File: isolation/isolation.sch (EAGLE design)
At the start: 85 parts, among them IC1 XTLV61048DBVR, IC2 SN74HC14PWR, IC3 SN74HCS32BQAR, IC4 SN74HCS08DYYR, IC5 FDN359BN, IC6 FDN359BN, IC7 FDN359BN, IC8 FDN359BN, J1 S4B-PH-K-S(LF)(SN), J2 S4B-PH-K-S(LF)(SN), J3 S2B-PH-K-S(LF)(SN), J4 S2B-PH-K-S(LF)(SN), J5 S2B-PH-K-S(LF)(SN)

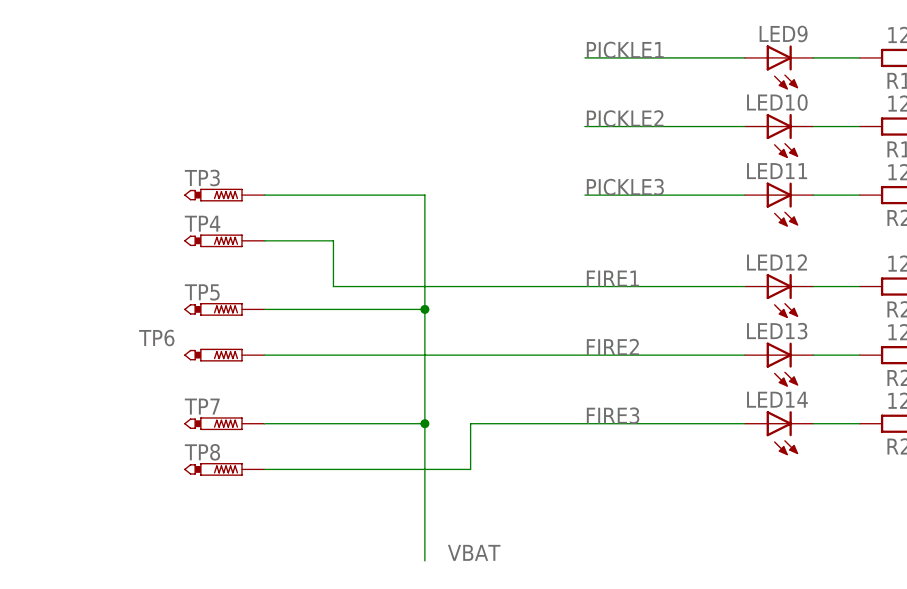
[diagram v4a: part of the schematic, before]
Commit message: placed shrunken components
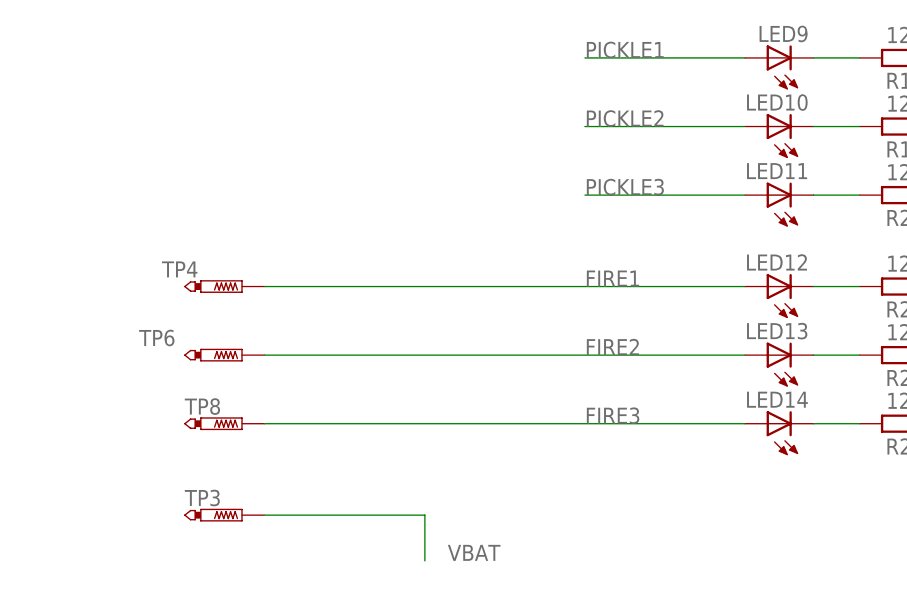
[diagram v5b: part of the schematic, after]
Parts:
- removed TP5, TP7: PTR1PAD1-13, testpad:PTR1PAD1-13
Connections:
- net VBAT: no longer TP5.TP, TP7.TP
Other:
- moved on the sheet: TP3, TP4, TP8
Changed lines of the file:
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@@
 <part name="TP3" library="testpad" library_urn="urn:adsk.eagle:library:385" deviceset="PTR1" device="PAD1-13" package3d_urn="urn:adsk.eagle:package:27946/1"/>
 <part name="TP4" library="testpad" library_urn="urn:adsk.eagle:library:385" deviceset="PTR1" device="PAD1-13" package3d_urn="urn:adsk.eagle:package:27946/1"/>
-<part name="TP5" library="testpad" library_urn="urn:adsk.eagle:library:385" deviceset="PTR1" device="PAD1-13" package3d_urn="urn:adsk.eagle:package:27946/1"/>
 <part name="TP6" library="testpad" library_urn="urn:adsk.eagle:library:385" deviceset="PTR1" device="PAD1-13" package3d_urn="urn:adsk.eagle:package:27946/1"/>
-<part name="TP7" library="testpad" library_urn="urn:adsk.eagle:library:385" deviceset="PTR1" device="PAD1-13" package3d_urn="urn:adsk.eagle:package:27946/1"/>
 <part name="TP8" library="testpad" library_urn="urn:adsk.eagle:library:385" deviceset="PTR1" device="PAD1-13" package3d_urn="urn:adsk.eagle:package:27946/1"/>
 <part name="TP9" library="testpad" library_urn="urn:adsk.eagle:library:385" deviceset="PTR1" device="PAD1-13" package3d_urn="urn:adsk.eagle:package:27946/1"/>
@@
 <attribute name="VALUE" x="96.52" y="-327.66" size="1.778" layer="96"/>
 </instance>
-<instance part="TP3" gate="G$1" x="40.64" y="-401.32" smashed="yes" rot="R270">
-<attribute name="NAME" x="34.29" y="-400.304" size="1.778" layer="95"/>
-<attribute name="TP_SIGNAL_NAME" x="38.1" y="-402.59" size="1.778" layer="97" rot="R270"/>
-</instance>
-<instance part="TP4" gate="G$1" x="40.64" y="-406.4" smashed="yes" rot="R270">
-<attribute name="NAME" x="34.29" y="-405.384" size="1.778" layer="95"/>
-<attribute name="TP_SIGNAL_NAME" x="38.1" y="-407.67" size="1.778" layer="97" rot="R270"/>
-</instance>
-<instance part="TP5" gate="G$1" x="40.64" y="-414.02" smashed="yes" rot="R270">
-<attribute name="NAME" x="34.29" y="-413.004" size="1.778" layer="95"/>
-<attribute name="TP_SIGNAL_NAME" x="38.1" y="-415.29" size="1.778" layer="97" rot="R270"/>
+<instance part="TP3" gate="G$1" x="40.64" y="-436.88" smashed="yes" rot="R270">
+<attribute name="NAME" x="34.29" y="-435.864" size="1.778" layer="95"/>
+<attribute name="TP_SIGNAL_NAME" x="38.1" y="-438.15" size="1.778" layer="97" rot="R270"/>
+</instance>
+<instance part="TP4" gate="G$1" x="40.64" y="-411.48" smashed="yes" rot="R270">
+<attribute name="NAME" x="31.75" y="-410.464" size="1.778" layer="95"/>
+<attribute name="TP_SIGNAL_NAME" x="38.1" y="-412.75" size="1.778" layer="97" rot="R270"/>
 </instance>
 <instance part="TP6" gate="G$1" x="40.64" y="-419.1" smashed="yes" rot="R270">
@@
 <attribute name="TP_SIGNAL_NAME" x="38.1" y="-420.37" size="1.778" layer="97" rot="R270"/>
 </instance>
-<instance part="TP7" gate="G$1" x="40.64" y="-426.72" smashed="yes" rot="R270">
+<instance part="TP8" gate="G$1" x="40.64" y="-426.72" smashed="yes" rot="R270">
 <attribute name="NAME" x="34.29" y="-425.704" size="1.778" layer="95"/>
 <attribute name="TP_SIGNAL_NAME" x="38.1" y="-427.99" size="1.778" layer="97" rot="R270"/>
-</instance>
-<instance part="TP8" gate="G$1" x="40.64" y="-431.8" smashed="yes" rot="R270">
-<attribute name="NAME" x="34.29" y="-430.784" size="1.778" layer="95"/>
-<attribute name="TP_SIGNAL_NAME" x="38.1" y="-433.07" size="1.778" layer="97" rot="R270"/>
 </instance>
 <instance part="TP9" gate="G$1" x="53.34" y="33.02" smashed="yes" rot="R270">
@@
 </segment>
 <segment>
-<wire x1="60.96" y1="-401.32" x2="60.96" y2="-414.02" width="0.1524" layer="91"/>
 <label x="63.5" y="-441.96" size="1.778" layer="95"/>
 <pinref part="TP3" gate="G$1" pin="TP"/>
-<wire x1="60.96" y1="-414.02" x2="60.96" y2="-426.72" width="0.1524" layer="91"/>
-<wire x1="60.96" y1="-426.72" x2="60.96" y2="-441.96" width="0.1524" layer="91"/>
-<wire x1="60.96" y1="-401.32" x2="43.18" y2="-401.32" width="0.1524" layer="91"/>
-<pinref part="TP5" gate="G$1" pin="TP"/>
-<wire x1="43.18" y1="-414.02" x2="60.96" y2="-414.02" width="0.1524" layer="91"/>
-<junction x="60.96" y="-414.02"/>
-<pinref part="TP7" gate="G$1" pin="TP"/>
-<wire x1="43.18" y1="-426.72" x2="60.96" y2="-426.72" width="0.1524" layer="91"/>
-<junction x="60.96" y="-426.72"/>
+<wire x1="60.96" y1="-436.88" x2="60.96" y2="-441.96" width="0.1524" layer="91"/>
+<wire x1="43.18" y1="-436.88" x2="60.96" y2="-436.88" width="0.1524" layer="91"/>
 </segment>
 </net>
@@
 <pinref part="LED12" gate="G$1" pin="A"/>
 <label x="78.74" y="-411.48" size="1.778" layer="95"/>
-<wire x1="96.52" y1="-411.48" x2="50.8" y2="-411.48" width="0.1524" layer="91"/>
-<wire x1="50.8" y1="-411.48" x2="50.8" y2="-406.4" width="0.1524" layer="91"/>
+<wire x1="96.52" y1="-411.48" x2="43.18" y2="-411.48" width="0.1524" layer="91"/>
 <pinref part="TP4" gate="G$1" pin="TP"/>
-<wire x1="50.8" y1="-406.4" x2="43.18" y2="-406.4" width="0.1524" layer="91"/>
 </segment>
 </net>
@@
 <pinref part="LED14" gate="G$1" pin="A"/>
 <label x="78.74" y="-426.72" size="1.778" layer="95"/>
-<wire x1="96.52" y1="-426.72" x2="66.04" y2="-426.72" width="0.1524" layer="91"/>
-<wire x1="66.04" y1="-426.72" x2="66.04" y2="-431.8" width="0.1524" layer="91"/>
+<wire x1="96.52" y1="-426.72" x2="43.18" y2="-426.72" width="0.1524" layer="91"/>
 <pinref part="TP8" gate="G$1" pin="TP"/>
-<wire x1="66.04" y1="-431.8" x2="43.18" y2="-431.8" width="0.1524" layer="91"/>
-</segment>
-</net>
+</segment>
+</net>

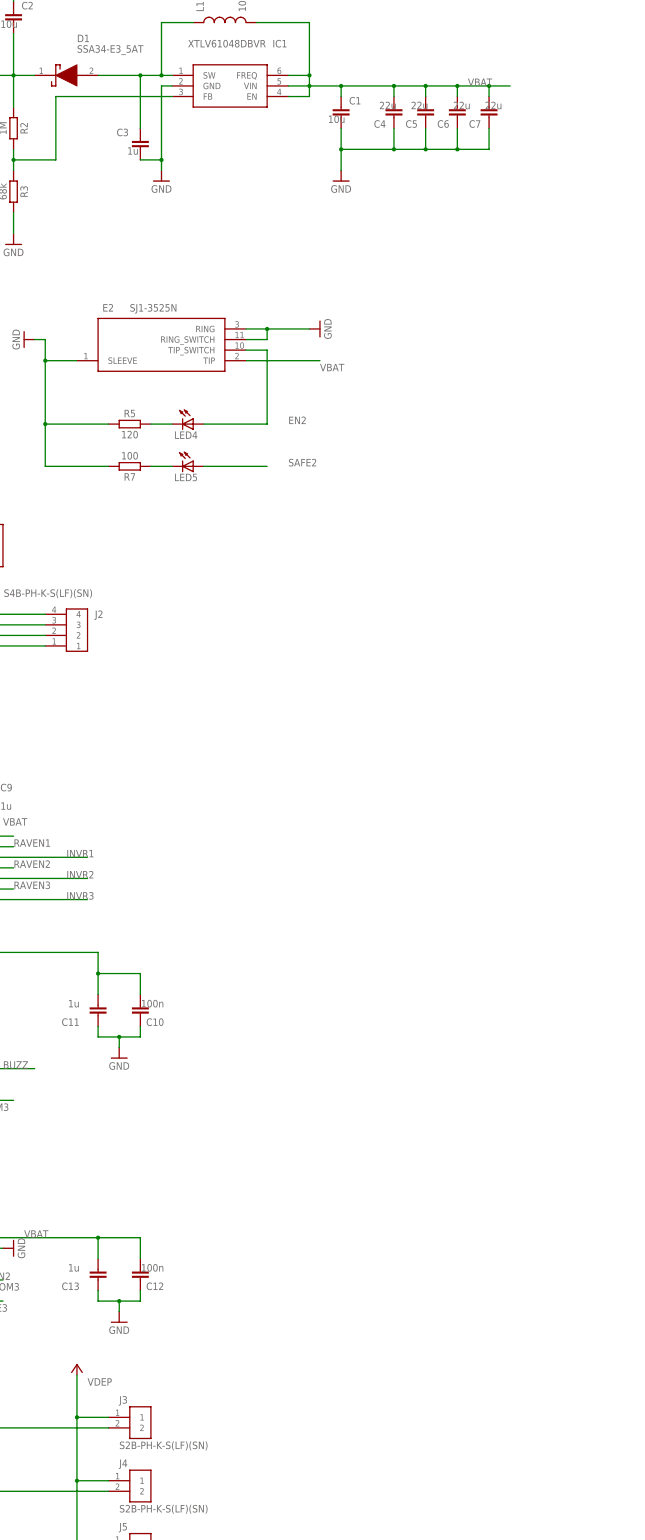
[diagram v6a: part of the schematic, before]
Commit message: add some bulk caps
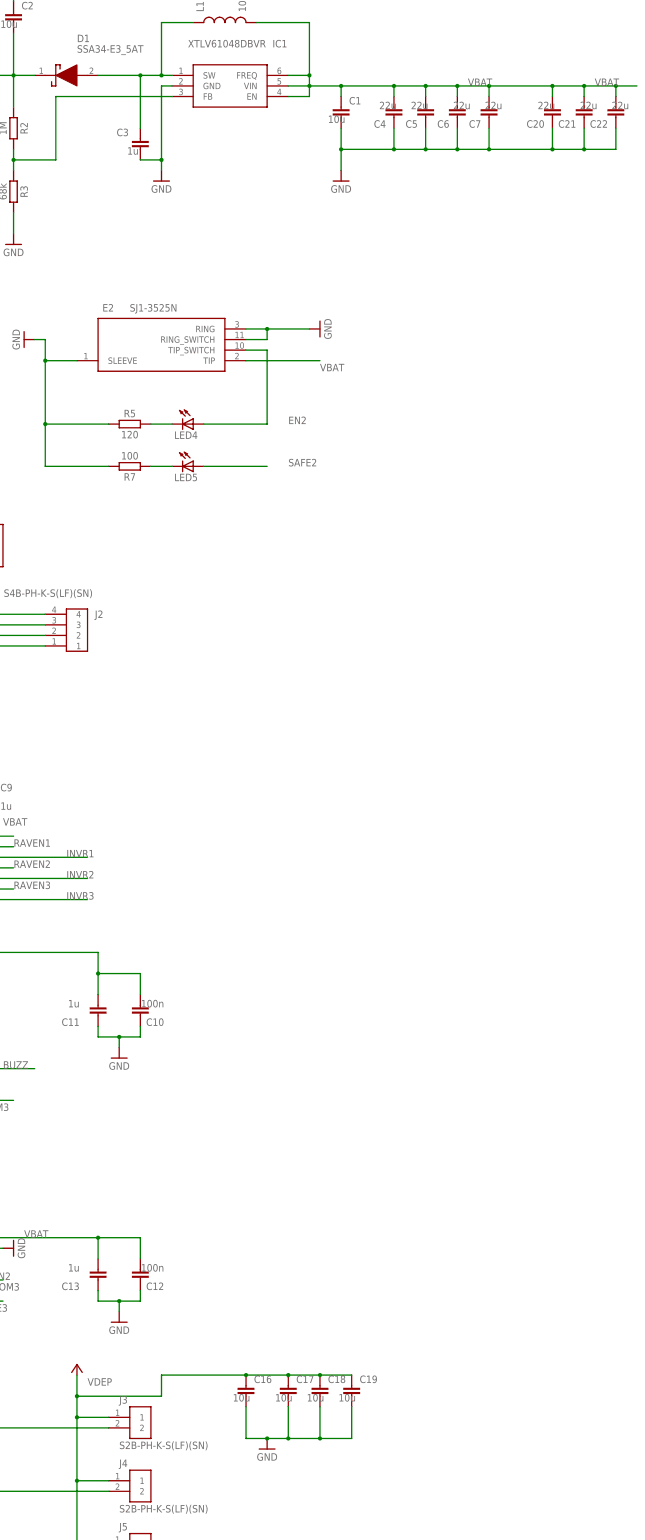
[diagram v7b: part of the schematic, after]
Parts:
- added C16, C17, C18, C19: 10u, Capacitor:C_CHIP-0603(1608-METRIC)
- added C20, C21, C22: 22u, Capacitor:C_CHIP-0603(1608-METRIC)
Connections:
- net GND: now also C16.2, C17.2, C18.2, C19.2, C20.1, C21.1, C22.1
- net VBAT: now also C20.2, C21.2, C22.2
- net VDEP: now also C16.1, C17.1, C18.1, C19.1
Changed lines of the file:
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@@
 <part name="TP8" library="testpad" library_urn="urn:adsk.eagle:library:385" deviceset="PTR1" device="PAD1-13" package3d_urn="urn:adsk.eagle:package:27946/1"/>
 <part name="TP9" library="testpad" library_urn="urn:adsk.eagle:library:385" deviceset="PTR1" device="PAD1-13" package3d_urn="urn:adsk.eagle:package:27946/1"/>
+<part name="C16" library="Capacitor" library_urn="urn:adsk.eagle:library:16290819" deviceset="C" device="CHIP-0603(1608-METRIC)" package3d_urn="urn:adsk.eagle:package:16290898/5" technology="_" value="10u"/>
+<part name="C17" library="Capacitor" library_urn="urn:adsk.eagle:library:16290819" deviceset="C" device="CHIP-0603(1608-METRIC)" package3d_urn="urn:adsk.eagle:package:16290898/5" technology="_" value="10u"/>
+<part name="SUPPLY28" library="Power_Symbols" library_urn="urn:adsk.eagle:library:16502351" deviceset="GND-BAR" device="" value="GND"/>
+<part name="C18" library="Capacitor" library_urn="urn:adsk.eagle:library:16290819" deviceset="C" device="CHIP-0603(1608-METRIC)" package3d_urn="urn:adsk.eagle:package:16290898/5" technology="_" value="10u"/>
+<part name="C19" library="Capacitor" library_urn="urn:adsk.eagle:library:16290819" deviceset="C" device="CHIP-0603(1608-METRIC)" package3d_urn="urn:adsk.eagle:package:16290898/5" technology="_" value="10u"/>
+<part name="C20" library="Capacitor" library_urn="urn:adsk.eagle:library:16290819" deviceset="C" device="CHIP-0603(1608-METRIC)" package3d_urn="urn:adsk.eagle:package:16290898/5" technology="_" value="22u"/>
+<part name="C21" library="Capacitor" library_urn="urn:adsk.eagle:library:16290819" deviceset="C" device="CHIP-0603(1608-METRIC)" package3d_urn="urn:adsk.eagle:package:16290898/5" technology="_" value="22u"/>
+<part name="C22" library="Capacitor" library_urn="urn:adsk.eagle:library:16290819" deviceset="C" device="CHIP-0603(1608-METRIC)" package3d_urn="urn:adsk.eagle:package:16290898/5" technology="_" value="22u"/>
 </parts>
 <sheets>
@@
 <attribute name="NAME" x="46.99" y="34.036" size="1.778" layer="95"/>
 <attribute name="TP_SIGNAL_NAME" x="50.8" y="31.75" size="1.778" layer="97" rot="R270"/>
+</instance>
+<instance part="C16" gate="G$1" x="127" y="-281.94" smashed="yes">
+<attribute name="NAME" x="128.905" y="-281.305" size="1.778" layer="95"/>
+<attribute name="VALUE" x="123.825" y="-285.75" size="1.778" layer="96"/>
+</instance>
+<instance part="C17" gate="G$1" x="137.16" y="-281.94" smashed="yes">
+<attribute name="NAME" x="139.065" y="-281.305" size="1.778" layer="95"/>
+<attribute name="VALUE" x="133.985" y="-285.75" size="1.778" layer="96"/>
+</instance>
+<instance part="SUPPLY28" gate="G$1" x="132.08" y="-297.18" smashed="yes">
+<attribute name="VALUE" x="132.08" y="-299.085" size="1.778" layer="96" align="center"/>
+</instance>
+<instance part="C18" gate="G$1" x="144.78" y="-281.94" smashed="yes">
+<attribute name="NAME" x="146.685" y="-281.305" size="1.778" layer="95"/>
+<attribute name="VALUE" x="141.605" y="-285.75" size="1.778" layer="96"/>
+</instance>
+<instance part="C19" gate="G$1" x="152.4" y="-281.94" smashed="yes">
+<attribute name="NAME" x="154.305" y="-281.305" size="1.778" layer="95"/>
+<attribute name="VALUE" x="149.225" y="-285.75" size="1.778" layer="96"/>
+</instance>
+<instance part="C20" gate="G$1" x="200.66" y="22.86" smashed="yes" rot="R180">
+<attribute name="NAME" x="198.755" y="22.225" size="1.778" layer="95" rot="R180"/>
+<attribute name="VALUE" x="201.295" y="26.67" size="1.778" layer="96" rot="R180"/>
+</instance>
+<instance part="C21" gate="G$1" x="208.28" y="22.86" smashed="yes" rot="R180">
+<attribute name="NAME" x="206.375" y="22.225" size="1.778" layer="95" rot="R180"/>
+<attribute name="VALUE" x="211.455" y="26.67" size="1.778" layer="96" rot="R180"/>
+</instance>
+<instance part="C22" gate="G$1" x="215.9" y="22.86" smashed="yes" rot="R180">
+<attribute name="NAME" x="213.995" y="22.225" size="1.778" layer="95" rot="R180"/>
+<attribute name="VALUE" x="219.075" y="26.67" size="1.778" layer="96" rot="R180"/>
 </instance>
 </instances>
@@
 <wire x1="185.42" y1="15.24" x2="177.8" y2="15.24" width="0.1524" layer="91"/>
 <junction x="177.8" y="15.24"/>
+<wire x1="208.28" y1="15.24" x2="200.66" y2="15.24" width="0.1524" layer="91"/>
+<pinref part="C20" gate="G$1" pin="1"/>
+<wire x1="200.66" y1="20.32" x2="200.66" y2="15.24" width="0.1524" layer="91"/>
+<pinref part="C21" gate="G$1" pin="1"/>
+<wire x1="208.28" y1="20.32" x2="208.28" y2="15.24" width="0.1524" layer="91"/>
+<pinref part="C22" gate="G$1" pin="1"/>
+<wire x1="215.9" y1="20.32" x2="215.9" y2="15.24" width="0.1524" layer="91"/>
+<wire x1="215.9" y1="15.24" x2="208.28" y2="15.24" width="0.1524" layer="91"/>
+<junction x="208.28" y="15.24"/>
+<wire x1="200.66" y1="15.24" x2="185.42" y2="15.24" width="0.1524" layer="91"/>
+<junction x="200.66" y="15.24"/>
+<junction x="185.42" y="15.24"/>
 </segment>
 <segment>
@@
 <wire x1="35.56" y1="-195.58" x2="35.56" y2="-182.88" width="0.1524" layer="91"/>
 </segment>
+<segment>
+<pinref part="C16" gate="G$1" pin="2"/>
+<wire x1="127" y1="-287.02" x2="127" y2="-294.64" width="0.1524" layer="91"/>
+<pinref part="SUPPLY28" gate="G$1" pin="GND"/>
+<wire x1="127" y1="-294.64" x2="132.08" y2="-294.64" width="0.1524" layer="91"/>
+<wire x1="132.08" y1="-294.64" x2="137.16" y2="-294.64" width="0.1524" layer="91"/>
+<junction x="132.08" y="-294.64"/>
+<pinref part="C17" gate="G$1" pin="2"/>
+<wire x1="137.16" y1="-294.64" x2="137.16" y2="-287.02" width="0.1524" layer="91"/>
+<pinref part="C18" gate="G$1" pin="2"/>
+<wire x1="144.78" y1="-287.02" x2="144.78" y2="-294.64" width="0.1524" layer="91"/>
+<wire x1="144.78" y1="-294.64" x2="137.16" y2="-294.64" width="0.1524" layer="91"/>
+<junction x="137.16" y="-294.64"/>
+<pinref part="C19" gate="G$1" pin="2"/>
+<wire x1="152.4" y1="-287.02" x2="152.4" y2="-294.64" width="0.1524" layer="91"/>
+<wire x1="152.4" y1="-294.64" x2="144.78" y2="-294.64" width="0.1524" layer="91"/>
+<junction x="144.78" y="-294.64"/>
+</segment>
 </net>
 <net name="VBAT" class="0">
@@
 <wire x1="162.56" y1="30.48" x2="149.86" y2="30.48" width="0.1524" layer="91"/>
 <wire x1="185.42" y1="27.94" x2="185.42" y2="30.48" width="0.1524" layer="91"/>
-<wire x1="185.42" y1="30.48" x2="190.5" y2="30.48" width="0.1524" layer="91"/>
 <junction x="185.42" y="30.48"/>
 <pinref part="C6" gate="G$1" pin="2"/>
@@
 <wire x1="162.56" y1="27.94" x2="162.56" y2="30.48" width="0.1524" layer="91"/>
 <junction x="162.56" y="30.48"/>
+<label x="210.82" y="30.48" size="1.778" layer="95"/>
+<wire x1="215.9" y1="30.48" x2="208.28" y2="30.48" width="0.1524" layer="91"/>
+<pinref part="C22" gate="G$1" pin="2"/>
+<wire x1="208.28" y1="30.48" x2="200.66" y2="30.48" width="0.1524" layer="91"/>
+<wire x1="215.9" y1="27.94" x2="215.9" y2="30.48" width="0.1524" layer="91"/>
+<wire x1="215.9" y1="30.48" x2="220.98" y2="30.48" width="0.1524" layer="91"/>
+<junction x="215.9" y="30.48"/>
+<pinref part="C21" gate="G$1" pin="2"/>
+<wire x1="208.28" y1="27.94" x2="208.28" y2="30.48" width="0.1524" layer="91"/>
+<junction x="208.28" y="30.48"/>
+<pinref part="C20" gate="G$1" pin="2"/>
+<wire x1="200.66" y1="27.94" x2="200.66" y2="30.48" width="0.1524" layer="91"/>
+<wire x1="185.42" y1="30.48" x2="200.66" y2="30.48" width="0.1524" layer="91"/>
+<junction x="200.66" y="30.48"/>
 </segment>
 <segment>
@@
 <wire x1="86.36" y1="-320.04" x2="86.36" y2="-304.8" width="0.1524" layer="91"/>
 <wire x1="86.36" y1="-304.8" x2="86.36" y2="-289.56" width="0.1524" layer="91"/>
-<wire x1="86.36" y1="-289.56" x2="86.36" y2="-279.4" width="0.1524" layer="91"/>
+<wire x1="86.36" y1="-289.56" x2="86.36" y2="-284.48" width="0.1524" layer="91"/>
+<wire x1="86.36" y1="-284.48" x2="86.36" y2="-279.4" width="0.1524" layer="91"/>
 <wire x1="93.98" y1="-289.56" x2="86.36" y2="-289.56" width="0.1524" layer="91"/>
 <junction x="86.36" y="-289.56"/>
@@
 <wire x1="93.98" y1="-320.04" x2="86.36" y2="-320.04" width="0.1524" layer="91"/>
 <junction x="86.36" y="-320.04"/>
+<pinref part="C16" gate="G$1" pin="1"/>
+<wire x1="127" y1="-279.4" x2="106.68" y2="-279.4" width="0.1524" layer="91"/>
+<wire x1="106.68" y1="-279.4" x2="106.68" y2="-284.48" width="0.1524" layer="91"/>
+<wire x1="106.68" y1="-284.48" x2="86.36" y2="-284.48" width="0.1524" layer="91"/>
+<junction x="86.36" y="-284.48"/>
+<pinref part="C17" gate="G$1" pin="1"/>
+<wire x1="127" y1="-279.4" x2="137.16" y2="-279.4" width="0.1524" layer="91"/>
+<junction x="127" y="-279.4"/>
+<pinref part="C18" gate="G$1" pin="1"/>
+<wire x1="137.16" y1="-279.4" x2="144.78" y2="-279.4" width="0.1524" layer="91"/>
+<junction x="137.16" y="-279.4"/>
+<pinref part="C19" gate="G$1" pin="1"/>
+<wire x1="144.78" y1="-279.4" x2="152.4" y2="-279.4" width="0.1524" layer="91"/>
+<junction x="144.78" y="-279.4"/>
 </segment>
 </net>

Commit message: label LEDs
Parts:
- LED1: value (none) -> LEDW
- LED10, LED11, LED12, LED13, LED14, LED6, LED7, LED8, LED9: value (none) -> LEDR
- LED2, LED4: value (none) -> LEDY
- LED3, LED5: value (none) -> LEDG
